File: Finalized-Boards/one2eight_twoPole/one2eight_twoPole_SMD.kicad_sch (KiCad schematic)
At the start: 20 parts

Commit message: Apply Matt's review changes to RTM, fanout and SRAM boards
SRAM: serial -> IDL_26_007 RevC - 09/2026 - CK/RS; vias untented (board-level);
GND zone 0.4 clearance / 0.1524 min width; In2 +3.3V stripe pulled back from
both board edges (tips 103.25 / 126.05) with 45-degree miters; +3.3V via moved
to (165.54, 125.92) and re-routed on F.Cu/B.Cu to clear GND (was 2 DRC errors);
C1/C2 0402 -> 0603 X7R in schematic and PCB; orphan teardrop + 2 zero-length
tracks removed.
Fanout: Matt's reworked layout (12 AWG input centred, both-side labels, 3 mm
shorter test points, D1/R1 as real reference designators, silk moved clear).
RTM: four 1812 1 A PPTCs, one per output; +5V pour full-board on F.Cu/In2,
GND on B.Cu/In1; 3.4 mm fused traces; zones extended past Edge.Cuts.
Removed stale pre-review gerbers/drills/layer PDFs (duplicates of Chris-Originals).
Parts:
- TP1, TP2: footprint Connector_Wire:SolderWire-4sqmm_1x01_D3mm_OD6mm_Relief -> 1_klm-sram-exp-lib:PTH_12AWG
- TP10, TP11, TP12, TP13, TP14, TP15, TP16, TP17, TP18, TP3, TP4, TP5, TP6, TP7, TP8, TP9: footprint Connector_Wire:SolderWire-0.5sqmm_1x01_D0.9mm_OD2.1mm_Relief -> 1_klm-sram-exp-lib:SolderWire-0.5sqmm_1x01_D0.9mm_OD2.1mm_Relief_3mm_shorter_version
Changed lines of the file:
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@@
 			)
 		)
-		(property "Footprint" "Connector_Wire:SolderWire-0.5sqmm_1x01_D0.9mm_OD2.1mm_Relief"
+		(property "Footprint" "1_klm-sram-exp-lib:SolderWire-0.5sqmm_1x01_D0.9mm_OD2.1mm_Relief_3mm_shorter_version"
 			(at 195.58 85.09 0)
 			(hide yes)
@@
 			)
 		)
-		(property "Footprint" "Connector_Wire:SolderWire-0.5sqmm_1x01_D0.9mm_OD2.1mm_Relief"
+		(property "Footprint" "1_klm-sram-exp-lib:SolderWire-0.5sqmm_1x01_D0.9mm_OD2.1mm_Relief_3mm_shorter_version"
 			(at 101.6 67.31 0)
 			(hide yes)
@@
 			)
 		)
-		(property "Footprint" "Connector_Wire:SolderWire-0.5sqmm_1x01_D0.9mm_OD2.1mm_Relief"
+		(property "Footprint" "1_klm-sram-exp-lib:SolderWire-0.5sqmm_1x01_D0.9mm_OD2.1mm_Relief_3mm_shorter_version"
 			(at 101.6 92.71 0)
 			(hide yes)
@@
 			)
 		)
-		(property "Footprint" "Connector_Wire:SolderWire-4sqmm_1x01_D3mm_OD6mm_Relief"
+		(property "Footprint" "1_klm-sram-exp-lib:PTH_12AWG"
 			(at 172.72 36.83 0)
 			(hide yes)
@@
 			)
 		)
-		(property "Footprint" "Connector_Wire:SolderWire-0.5sqmm_1x01_D0.9mm_OD2.1mm_Relief"
+		(property "Footprint" "1_klm-sram-exp-lib:SolderWire-0.5sqmm_1x01_D0.9mm_OD2.1mm_Relief_3mm_shorter_version"
 			(at 195.58 78.74 0)
 			(hide yes)
@@
 			)
 		)
-		(property "Footprint" "Connector_Wire:SolderWire-4sqmm_1x01_D3mm_OD6mm_Relief"
+		(property "Footprint" "1_klm-sram-exp-lib:PTH_12AWG"
 			(at 80.01 38.1 0)
 			(hide yes)
@@
 			)
 		)
-		(property "Footprint" "Connector_Wire:SolderWire-0.5sqmm_1x01_D0.9mm_OD2.1mm_Relief"
+		(property "Footprint" "1_klm-sram-exp-lib:SolderWire-0.5sqmm_1x01_D0.9mm_OD2.1mm_Relief_3mm_shorter_version"
 			(at 101.6 73.66 0)
 			(hide yes)
@@
 			)
 		)
-		(property "Footprint" "Connector_Wire:SolderWire-0.5sqmm_1x01_D0.9mm_OD2.1mm_Relief"
+		(property "Footprint" "1_klm-sram-exp-lib:SolderWire-0.5sqmm_1x01_D0.9mm_OD2.1mm_Relief_3mm_shorter_version"
 			(at 101.6 54.61 0)
 			(hide yes)
@@
 			)
 		)
-		(property "Footprint" "Connector_Wire:SolderWire-0.5sqmm_1x01_D0.9mm_OD2.1mm_Relief"
+		(property "Footprint" "1_klm-sram-exp-lib:SolderWire-0.5sqmm_1x01_D0.9mm_OD2.1mm_Relief_3mm_shorter_version"
 			(at 101.6 80.01 0)
 			(hide yes)
@@
 			)
 		)
-		(property "Footprint" "Connector_Wire:SolderWire-0.5sqmm_1x01_D0.9mm_OD2.1mm_Relief"
+		(property "Footprint" "1_klm-sram-exp-lib:SolderWire-0.5sqmm_1x01_D0.9mm_OD2.1mm_Relief_3mm_shorter_version"
 			(at 195.58 53.34 0)
 			(hide yes)
@@
 			)
 		)
-		(property "Footprint" "Connector_Wire:SolderWire-0.5sqmm_1x01_D0.9mm_OD2.1mm_Relief"
+		(property "Footprint" "1_klm-sram-exp-lib:SolderWire-0.5sqmm_1x01_D0.9mm_OD2.1mm_Relief_3mm_shorter_version"
 			(at 195.58 59.69 0)
 			(hide yes)
@@
 			)
 		)
-		(property "Footprint" "Connector_Wire:SolderWire-0.5sqmm_1x01_D0.9mm_OD2.1mm_Relief"
+		(property "Footprint" "1_klm-sram-exp-lib:SolderWire-0.5sqmm_1x01_D0.9mm_OD2.1mm_Relief_3mm_shorter_version"
 			(at 195.58 66.04 0)
 			(hide yes)
@@
 			)
 		)
-		(property "Footprint" "Connector_Wire:SolderWire-0.5sqmm_1x01_D0.9mm_OD2.1mm_Relief"
+		(property "Footprint" "1_klm-sram-exp-lib:SolderWire-0.5sqmm_1x01_D0.9mm_OD2.1mm_Relief_3mm_shorter_version"
 			(at 195.58 91.44 0)
 			(hide yes)
@@
 			)
 		)
-		(property "Footprint" "Connector_Wire:SolderWire-0.5sqmm_1x01_D0.9mm_OD2.1mm_Relief"
+		(property "Footprint" "1_klm-sram-exp-lib:SolderWire-0.5sqmm_1x01_D0.9mm_OD2.1mm_Relief_3mm_shorter_version"
 			(at 101.6 48.26 0)
 			(hide yes)
@@
 			)
 		)
-		(property "Footprint" "Connector_Wire:SolderWire-0.5sqmm_1x01_D0.9mm_OD2.1mm_Relief"
+		(property "Footprint" "1_klm-sram-exp-lib:SolderWire-0.5sqmm_1x01_D0.9mm_OD2.1mm_Relief_3mm_shorter_version"
 			(at 101.6 86.36 0)
 			(hide yes)
@@
 			)
 		)
-		(property "Footprint" "Connector_Wire:SolderWire-0.5sqmm_1x01_D0.9mm_OD2.1mm_Relief"
+		(property "Footprint" "1_klm-sram-exp-lib:SolderWire-0.5sqmm_1x01_D0.9mm_OD2.1mm_Relief_3mm_shorter_version"
 			(at 101.6 60.96 0)
 			(hide yes)
@@
 			)
 		)
-		(property "Footprint" "Connector_Wire:SolderWire-0.5sqmm_1x01_D0.9mm_OD2.1mm_Relief"
+		(property "Footprint" "1_klm-sram-exp-lib:SolderWire-0.5sqmm_1x01_D0.9mm_OD2.1mm_Relief_3mm_shorter_version"
 			(at 195.58 46.99 0)
 			(hide yes)
@@
 			)
 		)
-		(property "Footprint" "Connector_Wire:SolderWire-0.5sqmm_1x01_D0.9mm_OD2.1mm_Relief"
+		(property "Footprint" "1_klm-sram-exp-lib:SolderWire-0.5sqmm_1x01_D0.9mm_OD2.1mm_Relief_3mm_shorter_version"
 			(at 195.58 72.39 0)
 			(hide yes)

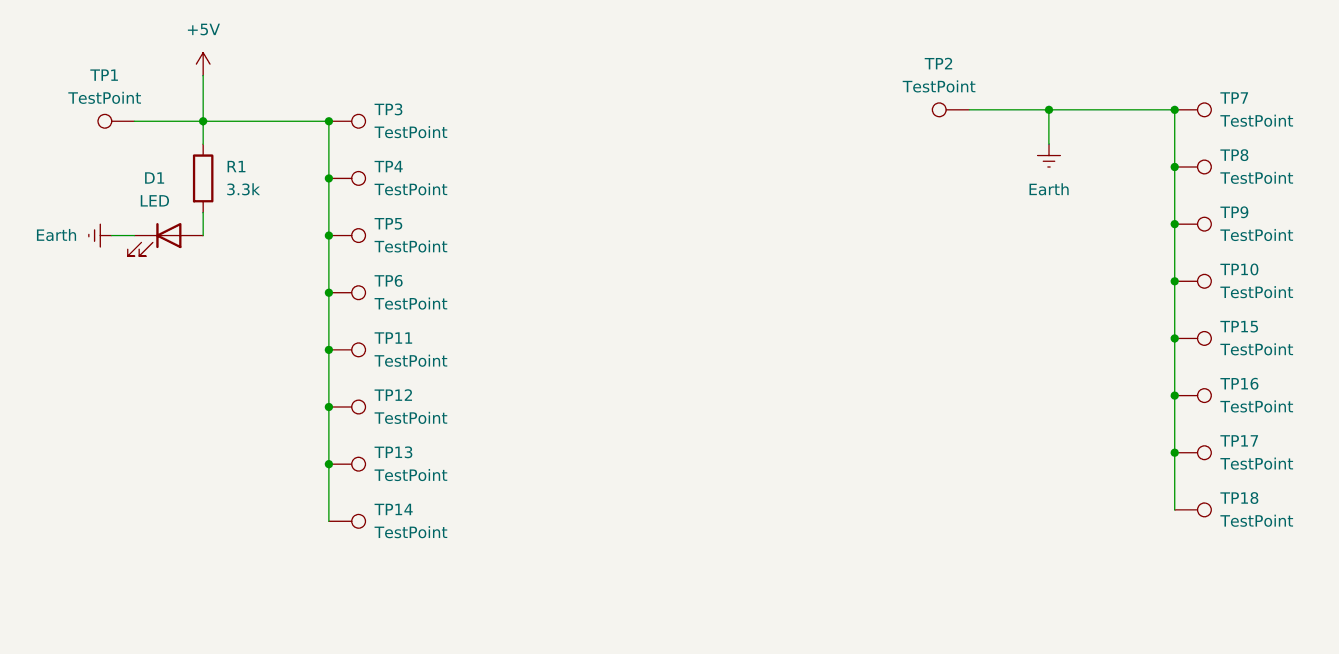
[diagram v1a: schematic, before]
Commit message: Matt's 9/17 review: RTM paired 5V/GND terminals, SRAM R1/R2 to 0603, fanout per-destination polyswitches; archive 9/16 boards
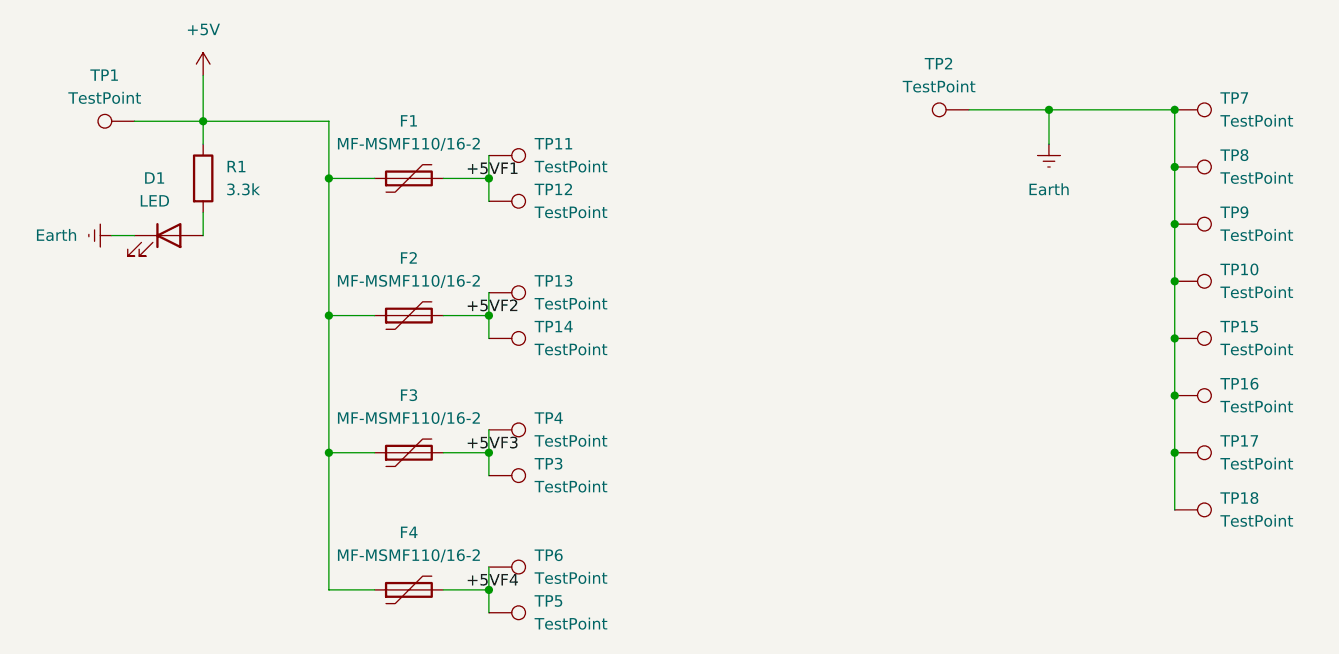
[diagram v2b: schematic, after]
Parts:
- added F1, F2, F3, F4: MF-MSMF110/16-2, Fuse:Fuse_1812_4532Metric, symbol Device:Polyfuse
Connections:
- net +5V: now also F1.1, F2.1, F3.1, F4.1; no longer TP11.1, TP12.1, TP13.1, TP14.1, TP3.1, TP4.1, TP5.1, TP6.1
- new net +5VF1: F1.2, TP11.1, TP12.1
- new net +5VF2: F2.2, TP13.1, TP14.1
- new net +5VF3: F3.2, TP3.1, TP4.1
- new net +5VF4: F4.2, TP5.1, TP6.1
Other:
- moved on the sheet: TP11, TP12, TP13, TP14, TP3, TP4, TP5, TP6

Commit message: Polyswitches sized to load: RTM F1-F4 MF-MSMF110/16-2 -> MF-MSMF030-2 (0.3 A), fanout F1-F4 -> MF-MSMF010-2 (0.1 A); refresh renders and DRC
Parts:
- F1, F2, F3, F4: value MF-MSMF110/16-2 -> MF-MSMF010-2
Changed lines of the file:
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@@
 			)
 		)
-		(property "Value" "MF-MSMF110/16-2"
+		(property "Value" "MF-MSMF010-2"
 			(at 110.49 45.72 90)
 			(show_name no)
@@
 			)
 		)
-		(property "Value" "MF-MSMF110/16-2"
+		(property "Value" "MF-MSMF010-2"
 			(at 110.49 60.96 90)
 			(show_name no)
@@
 			)
 		)
-		(property "Value" "MF-MSMF110/16-2"
+		(property "Value" "MF-MSMF010-2"
 			(at 110.49 76.2 90)
 			(show_name no)
@@
 			)
 		)
-		(property "Value" "MF-MSMF110/16-2"
+		(property "Value" "MF-MSMF010-2"
 			(at 110.49 91.44 90)
 			(show_name no)
